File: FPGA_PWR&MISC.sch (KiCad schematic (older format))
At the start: 95 parts, among them Q19 BSS139, U1 XC7A200T-FBG484

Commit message: SW2 placement changed, BOM cleared, FPGA boot, less ERC errors and wornings
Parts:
- removed R160: R0402_1K_1%_0.0625W_100PPM, RESC1005X40N, symbol Resistors_SMD:R0402_1K_1%_0.0625W_100PPM
- added R160: R0402_2K2_1%_0.0625W_100PPM, RESC1005X40N, symbol Resistors_SMD:R0402_2K2_1%_0.0625W_100PPM
- added R282: R0402_4K7_1%_0.0625W_100PPM, RESC1005X40N, symbol Resistors_SMD:R0402_4K7_1%_0.0625W_100PPM
- added R283, R284, R285: R0402_1K_1%_0.0625W_100PPM, RESC1005X40N, symbol Resistors_SMD:R0402_1K_1%_0.0625W_100PPM
- added R286, R287, R288: R0402_0R_JUMPER, RESC1005X40N, symbol Resistors_SMD:R0402_0R_JUMPER
- R162: config (none) -> dnf; ~ 300 -> DNP
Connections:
- wire segments 369 -> 386
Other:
- moved on the sheet: LD3, Q19, R159, R161, R162, R163

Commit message: BOM updated, 25MHz clock level fixed
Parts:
- PB1: symbol AMC_FMC_Carrier-PcbDoc-rescue:PB_TYCO_FSM2JSMA-Switches -> AMC_FMC_Carrier-PcbDoc-rescue:PB_TYCO_FSM2JSMA-Switches-AMC_FMC_Carrier-PcbDoc-rescue
- U1: symbol AMC_FMC_Carrier-PcbDoc-rescue:XC7A200T-FBG484-FPGA_Xilinx_Artix7 -> AMC_FMC_Carrier-PcbDoc-rescue:XC7A200T-FBG484-FPGA_Xilinx_Artix7-AMC_FMC_Carrier-PcbDoc-rescue
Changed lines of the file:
@@
 $EndDescr
 $Comp
-L AMC_FMC_Carrier-PcbDoc-rescue:XC7A200T-FBG484-FPGA_Xilinx_Artix7 U?
+L AMC_FMC_Carrier-PcbDoc-rescue:XC7A200T-FBG484-FPGA_Xilinx_Artix7-AMC_FMC_Carrier-PcbDoc-rescue U?
 U 5 1 5C5BFA2D
 P 11000 2150
@@
 $EndComp
 $Comp
-L AMC_FMC_Carrier-PcbDoc-rescue:XC7A200T-FBG484-FPGA_Xilinx_Artix7 U?
+L AMC_FMC_Carrier-PcbDoc-rescue:XC7A200T-FBG484-FPGA_Xilinx_Artix7-AMC_FMC_Carrier-PcbDoc-rescue U?
 U 6 1 5C5BFA33
 P 8450 5750
@@
 $EndComp
 $Comp
-L AMC_FMC_Carrier-PcbDoc-rescue:XC7A200T-FBG484-FPGA_Xilinx_Artix7 U?
+L AMC_FMC_Carrier-PcbDoc-rescue:XC7A200T-FBG484-FPGA_Xilinx_Artix7-AMC_FMC_Carrier-PcbDoc-rescue U?
 U 7 1 5C5BFA39
 P 3650 4450
@@
 	4700 2750 4700 2650
 $Comp
-L AMC_FMC_Carrier-PcbDoc-rescue:MGTAVCC-powerMG #PWR0440
+L AMC_FMC_Carrier-PcbDoc-rescue:MGTAVCC-powerMG-AMC_FMC_Carrier-PcbDoc-rescue #PWR0440
 U 1 1 5C5F4F86
 P 9450 1700
@@
 $EndComp
 $Comp
-L AMC_FMC_Carrier-PcbDoc-rescue:MGTAVTT-powerMG #PWR0426
+L AMC_FMC_Carrier-PcbDoc-rescue:MGTAVTT-powerMG-AMC_FMC_Carrier-PcbDoc-rescue #PWR0426
 U 1 1 5C5F55FB
 P 3250 9400
@@
 	12500 2150 12550 2150
 $Comp
-L AMC_FMC_Carrier-PcbDoc-rescue:VCCAUX-powerMG #PWR0420
+L AMC_FMC_Carrier-PcbDoc-rescue:VCCAUX-powerMG-AMC_FMC_Carrier-PcbDoc-rescue #PWR0420
 U 1 1 5C5FF42B
 P 2600 1450
@@
 $EndComp
 $Comp
-L AMC_FMC_Carrier-PcbDoc-rescue:VCCBRAM-powerMG #PWR0419
+L AMC_FMC_Carrier-PcbDoc-rescue:VCCBRAM-powerMG-AMC_FMC_Carrier-PcbDoc-rescue #PWR0419
 U 1 1 5C5FFC63
 P 2300 2450
@@
 	12550 1950 12550 1850
 $Comp
-L AMC_FMC_Carrier-PcbDoc-rescue:MGTAVTT-powerMG #PWR0453
+L AMC_FMC_Carrier-PcbDoc-rescue:MGTAVTT-powerMG-AMC_FMC_Carrier-PcbDoc-rescue #PWR0453
 U 1 1 5C618BA3
 P 13450 2450
@@
 $EndComp
 $Comp
-L AMC_FMC_Carrier-PcbDoc-rescue:VCCAUX-powerMG #PWR0421
+L AMC_FMC_Carrier-PcbDoc-rescue:VCCAUX-powerMG-AMC_FMC_Carrier-PcbDoc-rescue #PWR0421
 U 1 1 5C6DE6AD
 P 2600 10350
@@
 $EndComp
 $Comp
-L AMC_FMC_Carrier-PcbDoc-rescue:VCCBRAM-powerMG #PWR0412
+L AMC_FMC_Carrier-PcbDoc-rescue:VCCBRAM-powerMG-AMC_FMC_Carrier-PcbDoc-rescue #PWR0412
 U 1 1 5C6F2B54
 P 950 10300
@@
 $EndComp
 $Comp
-L AMC_FMC_Carrier-PcbDoc-rescue:MGTAVCC-powerMG #PWR0414
+L AMC_FMC_Carrier-PcbDoc-rescue:MGTAVCC-powerMG-AMC_FMC_Carrier-PcbDoc-rescue #PWR0414
 U 1 1 5C71121E
 P 1350 9400
@@
 	3250 9800 3250 9750
 $Comp
-L AMC_FMC_Carrier-PcbDoc-rescue:MGTAVTT-powerMG #PWR0424
+L AMC_FMC_Carrier-PcbDoc-rescue:MGTAVTT-powerMG-AMC_FMC_Carrier-PcbDoc-rescue #PWR0424
 U 1 1 5C961E72
 P 2800 9400
@@
 	2800 9750 2800 9800
 $Comp
-L AMC_FMC_Carrier-PcbDoc-rescue:MGTAVTT-powerMG #PWR0452
+L AMC_FMC_Carrier-PcbDoc-rescue:MGTAVTT-powerMG-AMC_FMC_Carrier-PcbDoc-rescue #PWR0452
 U 1 1 5C999EFD
 P 12550 1700
@@
 	900  9750 900  9800
 $Comp
-L AMC_FMC_Carrier-PcbDoc-rescue:MGTAVCC-powerMG #PWR0410
+L AMC_FMC_Carrier-PcbDoc-rescue:MGTAVCC-powerMG-AMC_FMC_Carrier-PcbDoc-rescue #PWR0410
 U 1 1 5C9F2FA3
 P 900 9400
@@
 PROG_B
 $Comp
-L AMC_FMC_Carrier-PcbDoc-rescue:PB_TYCO_FSM2JSMA-Switches PB1
+L AMC_FMC_Carrier-PcbDoc-rescue:PB_TYCO_FSM2JSMA-Switches-AMC_FMC_Carrier-PcbDoc-rescue PB1
 U 1 1 5C6A56F0
 P 11350 6550

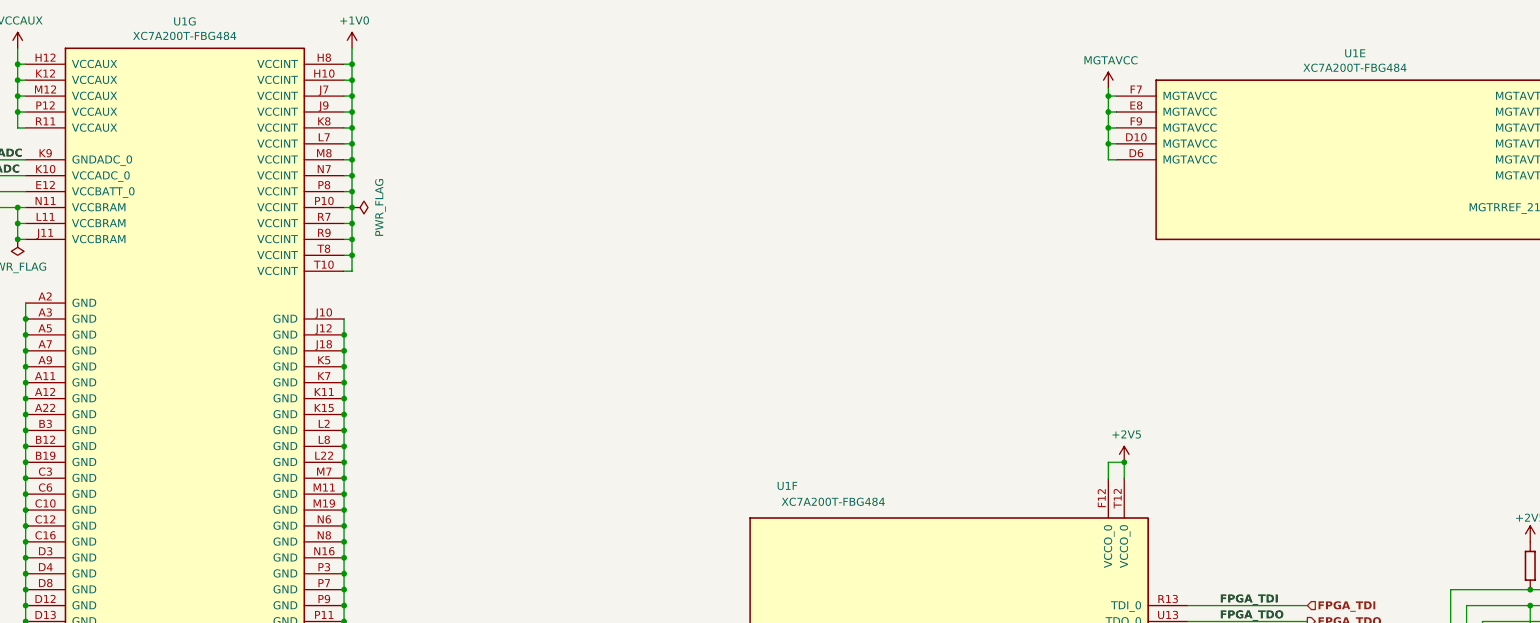
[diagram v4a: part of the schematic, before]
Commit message: BOM configuration file edited, updated Marble picture, some components part number changed
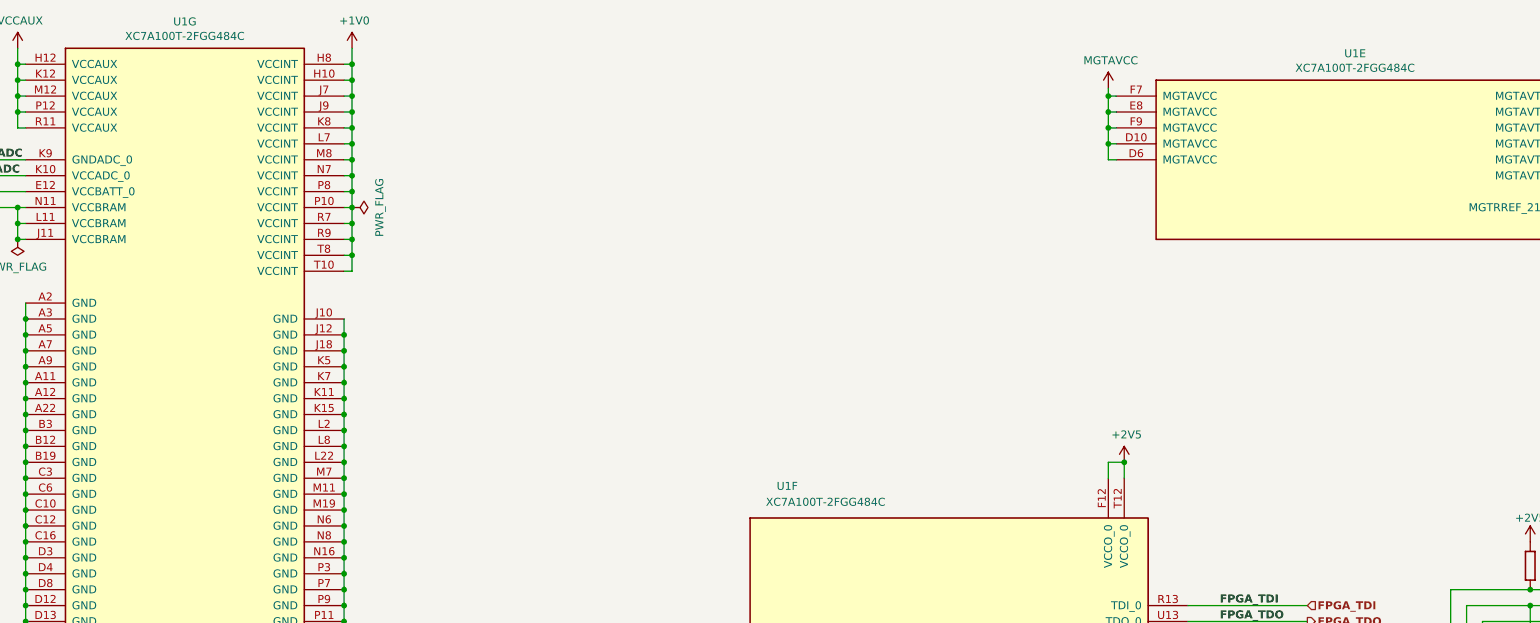
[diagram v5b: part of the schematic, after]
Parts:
- Q19: Manufacturer Part Number BSS139 -> BSS139H6327XTSA1
- U1: value XC7A200T-FBG484 -> XC7A100T-2FGG484C; Manufacturer Part Number (none) -> XC7A100T-2FGG484C
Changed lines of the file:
@@
 $Descr A3 16535 11693
 encoding utf-8
-Sheet 18 25
+Sheet 17 25
 Title "Marble"
 Date "2019-01-16"
@@
 AR Path="/5C907554/5C417BCB/5C5BFA2D" Ref="U1"  Part="5"
 F 0 "U1" H 11000 2817 50  0000 C CNN
-F 1 "XC7A200T-FBG484" H 11000 2726 50  0000 C CNN
+F 1 "XC7A100T-2FGG484C" H 11000 2726 50  0000 C CNN
 F 2 "ICs And Semiconductors SMD_BGA:BGA484C100P22X22_2300X2300X240" H 11000 2150 50  0001 C CNN
 F 3 "" H 11000 2150 50  0000 C CNN
+F 4 "XC7A100T-2FGG484C" H 11000 2150 50  0001 C CNN "Manufacturer Part Number"
 	5    11000 2150
 	1    0    0    -1
@@
 AR Path="/5C907554/5C417BCB/5C5BFA33" Ref="U1"  Part="6"
 F 0 "U1" H 7500 7300 50  0000 R CNN
-F 1 "XC7A200T-FBG484" H 8050 7200 50  0000 R CNN
+F 1 "XC7A100T-2FGG484C" H 8050 7200 50  0000 R CNN
 F 2 "ICs And Semiconductors SMD_BGA:BGA484C100P22X22_2300X2300X240" H 8450 5750 50  0001 C CNN
 F 3 "" H 8450 5750 50  0000 C CNN
+F 4 "XC7A100T-2FGG484C" H 8450 5750 50  0001 C CNN "Manufacturer Part Number"
 	6    8450 5750
 	1    0    0    -1
@@
 AR Path="/5C907554/5C417BCB/5C5BFA39" Ref="U1"  Part="7"
 F 0 "U1" H 3650 7617 50  0000 C CNN
-F 1 "XC7A200T-FBG484" H 3650 7526 50  0000 C CNN
+F 1 "XC7A100T-2FGG484C" H 3650 7526 50  0000 C CNN
 F 2 "ICs And Semiconductors SMD_BGA:BGA484C100P22X22_2300X2300X240" H 3650 4450 50  0001 C CNN
 F 3 "" H 3650 4450 50  0000 C CNN
+F 4 "XC7A100T-2FGG484C" H 3650 4450 50  0001 C CNN "Manufacturer Part Number"
 	7    3650 4450
 	1    0    0    -1
@@
 F 13 "250V 30mA N-Channel  SIPMOS® Small-Signal-Transistor" H 15150 3720 60  0001 L CNN "Part Description"
 F 14 "INFINEON" H 15150 3630 60  0001 L CNN "Manufacturer"
-F 15 "BSS139" H 15150 3540 60  0001 L CNN "Manufacturer Part Number"
+F 15 "BSS139H6327XTSA1" H 15150 3540 60  0001 L CNN "Manufacturer Part Number"
 F 16 "3" H 15150 3450 60  0001 L CNN "Pin Count"
 F 17 "SOT23-3" H 15150 3360 60  0001 L CNN "Case"

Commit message: applied all required amendments to the project
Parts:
- Q19: value BSS139 -> BSS138LT1G; footprint SOT95P240X110-3N -> ICs And Semiconductors SMD:SOT95P240X110-3N; symbol Transistors:BSS139 -> Transistors:BSS138LT1G; Comment =Device -> BSS138LT1G; ComponentHeight 1.1mm -> 1.11mm; ComponentLink1Description ~~ -> (none); ComponentLink2Description ~~ -> (none); CreateDate 09/23/14 00:00:00 -> 03/23/09 00:00:00; Database Table Name (none) -> Transistors; Device BSS139 -> BSS138LT1G; Footprint Library (none) -> ICs And Semiconductors SMD; LatestRevisionDate 09/23/14 00:00:00 -> 03/23/09 00:00:00; Library Name ICs And Semiconductors SMD -> ICs And Semiconductors.DbLib; Manufacturer INFINEON -> ON SEMICONDUCTOR; Manufacturer Part Number BSS139H6327XTSA1 -> BSS138LT1G; Part Description 250V 30mA N-Channel SIPMOS® Small-Signal-Transistor -> 50V 200mA N-Channel Enhancement Mode Field-Effect Transistor; Part Number BSS139 -> BSS138LT1G; SCEM (none) -> (none); Sense Comment ~~ -> (none); Status ~~ -> (none); Status Comment ~~ -> (none)
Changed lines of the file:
@@
 EESchema Schematic File Version 4
 LIBS:AMC_FMC_Carrier-PcbDoc-cache
-EELAYER 29 0
+EELAYER 30 0
 EELAYER END
 $Descr A3 16535 11693
@@
 $EndComp
 $Comp
-L Transistors:BSS139 Q19
+L Transistors:BSS138LT1G Q19
 U 1 1 5D220E28
 P 15150 5200
 F 0 "Q19" H 15469 5296 50  0000 L CNN
-F 1 "BSS139" H 15469 5205 50  0000 L CNN
-F 2 "SOT95P240X110-3N" H 15150 3990 60  0001 L CNN
+F 1 "BSS138LT1G" H 15469 5205 50  0000 L CNN
+F 2 "ICs And Semiconductors SMD:SOT95P240X110-3N" H 15150 3990 60  0001 L CNN
 F 3 "\\\\cern.ch\\dfs\\Applications\\Altium\\Datasheets\\BSS139.pdf" H 15150 4710 60  0001 L CNN
-F 4 "BSS139" H 15150 4620 60  0001 L CNN "Part Number"
+F 4 "BSS138LT1G" H 15150 4620 60  0001 L CNN "Part Number"
 F 5 "N-MOSFET-D 1G 2S 3D" H 15150 4530 60  0001 L CNN "Library Ref"
 F 6 "SchLib\\Transistors.SchLib" H 15150 4440 60  0001 L CNN "Library Path"
-F 7 "=Device" H 15150 4350 60  0001 L CNN "Comment"
+F 7 "BSS138LT1G" H 15150 4350 60  0001 L CNN "Comment"
 F 8 "Standard" H 15150 4260 60  0001 L CNN "Component Kind"
 F 9 "Standard" H 15150 4170 60  0001 L CNN "Component Type"
-F 10 "BSS139" H 15150 4080 60  0001 L CNN "Device"
+F 10 "BSS138LT1G" H 15150 4080 60  0001 L CNN "Device"
 F 11 "SOT23 3-Leads, Pitch 0.95mm - Body 1.4x3mm, IPC Medium Density" H 15150 3900 60  0001 L CNN "PackageDescription"
-F 12 "~~" H 15150 3810 60  0001 L CNN "Status"
-F 13 "250V 30mA N-Channel  SIPMOS® Small-Signal-Transistor" H 15150 3720 60  0001 L CNN "Part Description"
-F 14 "INFINEON" H 15150 3630 60  0001 L CNN "Manufacturer"
-F 15 "BSS139H6327XTSA1" H 15150 3540 60  0001 L CNN "Manufacturer Part Number"
+F 12 " " H 15150 3810 60  0001 L CNN "Status"
+F 13 "50V 200mA N-Channel Enhancement Mode Field-Effect Transistor" H 15150 3720 60  0001 L CNN "Part Description"
+F 14 "ON SEMICONDUCTOR" H 15150 3630 60  0001 L CNN "Manufacturer"
+F 15 "BSS138LT1G" H 15150 3540 60  0001 L CNN "Manufacturer Part Number"
 F 16 "3" H 15150 3450 60  0001 L CNN "Pin Count"
 F 17 "SOT23-3" H 15150 3360 60  0001 L CNN "Case"
@@
 F 21 "Yes" H 15150 3000 60  0001 L CNN "SMD"
 F 22 "No" H 15150 2910 60  0001 L CNN "Sense"
-F 23 "~~" H 15150 2820 60  0001 L CNN "Sense Comment"
+F 23 " " H 15150 2820 60  0001 L CNN "Sense Comment"
 F 24 "No" H 15150 2730 60  0001 L CNN "Bonding"
-F 25 "~~" H 15150 2640 60  0001 L CNN "Status Comment"
-F 26 "1.1mm" H 15150 2550 60  0001 L CNN "ComponentHeight"
+F 25 " " H 15150 2640 60  0001 L CNN "Status Comment"
+F 26 "1.11mm" H 15150 2550 60  0001 L CNN "ComponentHeight"
 F 27 "PcbLib\\ICs And Semiconductors SMD.PcbLib" H 15150 2460 60  0001 L CNN "Footprint Path"
 F 28 "SOT95P240X110-3N" H 15150 2370 60  0001 L CNN "Footprint Ref"
 F 29 "\\\\cern.ch\\dfs\\Applications\\Altium\\Datasheets\\BSS139.pdf" H 15150 2280 60  0001 L CNN "HelpURL"
 F 30 "~~" H 15150 2190 60  0001 L CNN "ComponentLink1URL"
-F 31 "~~" H 15150 2100 60  0001 L CNN "ComponentLink1Description"
+F 31 " " H 15150 2100 60  0001 L CNN "ComponentLink1Description"
 F 32 "~~" H 15150 2010 60  0001 L CNN "ComponentLink2URL"
-F 33 "~~" H 15150 1920 60  0001 L CNN "ComponentLink2Description"
+F 33 " " H 15150 1920 60  0001 L CNN "ComponentLink2Description"
 F 34 "CERN DEM JLC" H 15150 1830 60  0001 L CNN "Author"
-F 35 "09/23/14 00:00:00" H 15150 1740 60  0001 L CNN "CreateDate"
-F 36 "09/23/14 00:00:00" H 15150 1650 60  0001 L CNN "LatestRevisionDate"
-F 37 "ICs And Semiconductors SMD" H 15150 1560 60  0001 L CNN "Library Name"
+F 35 "03/23/09 00:00:00" H 15150 1740 60  0001 L CNN "CreateDate"
+F 36 "03/23/09 00:00:00" H 15150 1650 60  0001 L CNN "LatestRevisionDate"
+F 37 "ICs And Semiconductors.DbLib" H 15150 1560 60  0001 L CNN "Library Name"
 F 38 "This work is licensed under the Creative Commons CC-BY-SA 4.0 License. To the extent that circuit schematics that use Licensed Material can be considered to be ‘Adapted Material’, then the copyright holder waives article 3.b of the license with respect to these schematics." H 15150 1470 60  0001 L CNN "License"
+F 39 "Transistors" H 15150 5200 50  0001 C CNN "Database Table Name"
+F 40 "ICs And Semiconductors SMD" H 15150 5200 50  0001 C CNN "Footprint Library"
+F 41 " " H 15150 5200 50  0001 C CNN "SCEM"
 	1    15150 5200
 	1    0    0    -1

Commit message: Rename library AMC_FMC_Carrier-PcbDoc-rescue as marble_misc
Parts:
- PB1: symbol AMC_FMC_Carrier-PcbDoc-rescue:PB_TYCO_FSM2JSMA-Switches-AMC_FMC_Carrier-PcbDoc-rescue -> marble_misc:PB_TYCO_FSM2JSMA-Switches-AMC_FMC_Carrier-PcbDoc-rescue
- U1: symbol AMC_FMC_Carrier-PcbDoc-rescue:XC7A200T-FBG484-FPGA_Xilinx_Artix7-AMC_FMC_Carrier-PcbDoc-rescue -> marble_misc:XC7A200T-FBG484-FPGA_Xilinx_Artix7-AMC_FMC_Carrier-PcbDoc-rescue
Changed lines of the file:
@@
 $EndDescr
 $Comp
-L AMC_FMC_Carrier-PcbDoc-rescue:XC7A200T-FBG484-FPGA_Xilinx_Artix7-AMC_FMC_Carrier-PcbDoc-rescue U?
+L marble_misc:XC7A200T-FBG484-FPGA_Xilinx_Artix7-AMC_FMC_Carrier-PcbDoc-rescue U?
 U 5 1 5C5BFA2D
 P 11000 2150
@@
 $EndComp
 $Comp
-L AMC_FMC_Carrier-PcbDoc-rescue:XC7A200T-FBG484-FPGA_Xilinx_Artix7-AMC_FMC_Carrier-PcbDoc-rescue U?
+L marble_misc:XC7A200T-FBG484-FPGA_Xilinx_Artix7-AMC_FMC_Carrier-PcbDoc-rescue U?
 U 6 1 5C5BFA33
 P 8450 5750
@@
 $EndComp
 $Comp
-L AMC_FMC_Carrier-PcbDoc-rescue:XC7A200T-FBG484-FPGA_Xilinx_Artix7-AMC_FMC_Carrier-PcbDoc-rescue U?
+L marble_misc:XC7A200T-FBG484-FPGA_Xilinx_Artix7-AMC_FMC_Carrier-PcbDoc-rescue U?
 U 7 1 5C5BFA39
 P 3650 4450
@@
 	4700 2750 4700 2650
 $Comp
-L AMC_FMC_Carrier-PcbDoc-rescue:MGTAVCC-powerMG-AMC_FMC_Carrier-PcbDoc-rescue #PWR0440
+L marble_misc:MGTAVCC-powerMG-AMC_FMC_Carrier-PcbDoc-rescue #PWR0440
 U 1 1 5C5F4F86
 P 9450 1700
@@
 $EndComp
 $Comp
-L AMC_FMC_Carrier-PcbDoc-rescue:MGTAVTT-powerMG-AMC_FMC_Carrier-PcbDoc-rescue #PWR0426
+L marble_misc:MGTAVTT-powerMG-AMC_FMC_Carrier-PcbDoc-rescue #PWR0426
 U 1 1 5C5F55FB
 P 3250 9400
@@
 	12500 2150 12550 2150
 $Comp
-L AMC_FMC_Carrier-PcbDoc-rescue:VCCAUX-powerMG-AMC_FMC_Carrier-PcbDoc-rescue #PWR0420
+L marble_misc:VCCAUX-powerMG-AMC_FMC_Carrier-PcbDoc-rescue #PWR0420
 U 1 1 5C5FF42B
 P 2600 1450
@@
 $EndComp
 $Comp
-L AMC_FMC_Carrier-PcbDoc-rescue:VCCBRAM-powerMG-AMC_FMC_Carrier-PcbDoc-rescue #PWR0419
+L marble_misc:VCCBRAM-powerMG-AMC_FMC_Carrier-PcbDoc-rescue #PWR0419
 U 1 1 5C5FFC63
 P 2300 2450
@@
 	12550 1950 12550 1850
 $Comp
-L AMC_FMC_Carrier-PcbDoc-rescue:MGTAVTT-powerMG-AMC_FMC_Carrier-PcbDoc-rescue #PWR0453
+L marble_misc:MGTAVTT-powerMG-AMC_FMC_Carrier-PcbDoc-rescue #PWR0453
 U 1 1 5C618BA3
 P 13450 2450
@@
 $EndComp
 $Comp
-L AMC_FMC_Carrier-PcbDoc-rescue:VCCAUX-powerMG-AMC_FMC_Carrier-PcbDoc-rescue #PWR0421
+L marble_misc:VCCAUX-powerMG-AMC_FMC_Carrier-PcbDoc-rescue #PWR0421
 U 1 1 5C6DE6AD
 P 2600 10350
@@
 $EndComp
 $Comp
-L AMC_FMC_Carrier-PcbDoc-rescue:VCCBRAM-powerMG-AMC_FMC_Carrier-PcbDoc-rescue #PWR0412
+L marble_misc:VCCBRAM-powerMG-AMC_FMC_Carrier-PcbDoc-rescue #PWR0412
 U 1 1 5C6F2B54
 P 950 10300
@@
 $EndComp
 $Comp
-L AMC_FMC_Carrier-PcbDoc-rescue:MGTAVCC-powerMG-AMC_FMC_Carrier-PcbDoc-rescue #PWR0414
+L marble_misc:MGTAVCC-powerMG-AMC_FMC_Carrier-PcbDoc-rescue #PWR0414
 U 1 1 5C71121E
 P 1350 9400
@@
 	3250 9800 3250 9750
 $Comp
-L AMC_FMC_Carrier-PcbDoc-rescue:MGTAVTT-powerMG-AMC_FMC_Carrier-PcbDoc-rescue #PWR0424
+L marble_misc:MGTAVTT-powerMG-AMC_FMC_Carrier-PcbDoc-rescue #PWR0424
 U 1 1 5C961E72
 P 2800 9400
@@
 	2800 9750 2800 9800
 $Comp
-L AMC_FMC_Carrier-PcbDoc-rescue:MGTAVTT-powerMG-AMC_FMC_Carrier-PcbDoc-rescue #PWR0452
+L marble_misc:MGTAVTT-powerMG-AMC_FMC_Carrier-PcbDoc-rescue #PWR0452
 U 1 1 5C999EFD
 P 12550 1700
@@
 	900  9750 900  9800
 $Comp
-L AMC_FMC_Carrier-PcbDoc-rescue:MGTAVCC-powerMG-AMC_FMC_Carrier-PcbDoc-rescue #PWR0410
+L marble_misc:MGTAVCC-powerMG-AMC_FMC_Carrier-PcbDoc-rescue #PWR0410
 U 1 1 5C9F2FA3
 P 900 9400
@@
 PROG_B
 $Comp
-L AMC_FMC_Carrier-PcbDoc-rescue:PB_TYCO_FSM2JSMA-Switches-AMC_FMC_Carrier-PcbDoc-rescue PB1
+L marble_misc:PB_TYCO_FSM2JSMA-Switches-AMC_FMC_Carrier-PcbDoc-rescue PB1
 U 1 1 5C6A56F0
 P 11350 6550

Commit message: Strip extraneous AMC_FMC_Carrier-PcbDoc-rescue and powerMG from symbol names
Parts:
- PB1: symbol marble_misc:PB_TYCO_FSM2JSMA-Switches-AMC_FMC_Carrier-PcbDoc-rescue -> marble_misc:PB_TYCO_FSM2JSMA-Switches
- U1: symbol marble_misc:XC7A200T-FBG484-FPGA_Xilinx_Artix7-AMC_FMC_Carrier-PcbDoc-rescue -> marble_misc:XC7A200T-FBG484-FPGA_Xilinx_Artix7
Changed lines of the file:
@@
 $EndDescr
 $Comp
-L marble_misc:XC7A200T-FBG484-FPGA_Xilinx_Artix7-AMC_FMC_Carrier-PcbDoc-rescue U?
+L marble_misc:XC7A200T-FBG484-FPGA_Xilinx_Artix7 U?
 U 5 1 5C5BFA2D
 P 11000 2150
@@
 $EndComp
 $Comp
-L marble_misc:XC7A200T-FBG484-FPGA_Xilinx_Artix7-AMC_FMC_Carrier-PcbDoc-rescue U?
+L marble_misc:XC7A200T-FBG484-FPGA_Xilinx_Artix7 U?
 U 6 1 5C5BFA33
 P 8450 5750
@@
 $EndComp
 $Comp
-L marble_misc:XC7A200T-FBG484-FPGA_Xilinx_Artix7-AMC_FMC_Carrier-PcbDoc-rescue U?
+L marble_misc:XC7A200T-FBG484-FPGA_Xilinx_Artix7 U?
 U 7 1 5C5BFA39
 P 3650 4450
@@
 	4700 2750 4700 2650
 $Comp
-L marble_misc:MGTAVCC-powerMG-AMC_FMC_Carrier-PcbDoc-rescue #PWR0440
+L marble_misc:MGTAVCC #PWR0440
 U 1 1 5C5F4F86
 P 9450 1700
@@
 $EndComp
 $Comp
-L marble_misc:MGTAVTT-powerMG-AMC_FMC_Carrier-PcbDoc-rescue #PWR0426
+L marble_misc:MGTAVTT #PWR0426
 U 1 1 5C5F55FB
 P 3250 9400
@@
 	12500 2150 12550 2150
 $Comp
-L marble_misc:VCCAUX-powerMG-AMC_FMC_Carrier-PcbDoc-rescue #PWR0420
+L marble_misc:VCCAUX #PWR0420
 U 1 1 5C5FF42B
 P 2600 1450
@@
 $EndComp
 $Comp
-L marble_misc:VCCBRAM-powerMG-AMC_FMC_Carrier-PcbDoc-rescue #PWR0419
+L marble_misc:VCCBRAM #PWR0419
 U 1 1 5C5FFC63
 P 2300 2450
@@
 	12550 1950 12550 1850
 $Comp
-L marble_misc:MGTAVTT-powerMG-AMC_FMC_Carrier-PcbDoc-rescue #PWR0453
+L marble_misc:MGTAVTT #PWR0453
 U 1 1 5C618BA3
 P 13450 2450
@@
 $EndComp
 $Comp
-L marble_misc:VCCAUX-powerMG-AMC_FMC_Carrier-PcbDoc-rescue #PWR0421
+L marble_misc:VCCAUX #PWR0421
 U 1 1 5C6DE6AD
 P 2600 10350
@@
 $EndComp
 $Comp
-L marble_misc:VCCBRAM-powerMG-AMC_FMC_Carrier-PcbDoc-rescue #PWR0412
+L marble_misc:VCCBRAM #PWR0412
 U 1 1 5C6F2B54
 P 950 10300
@@
 $EndComp
 $Comp
-L marble_misc:MGTAVCC-powerMG-AMC_FMC_Carrier-PcbDoc-rescue #PWR0414
+L marble_misc:MGTAVCC #PWR0414
 U 1 1 5C71121E
 P 1350 9400
@@
 	3250 9800 3250 9750
 $Comp
-L marble_misc:MGTAVTT-powerMG-AMC_FMC_Carrier-PcbDoc-rescue #PWR0424
+L marble_misc:MGTAVTT #PWR0424
 U 1 1 5C961E72
 P 2800 9400
@@
 	2800 9750 2800 9800
 $Comp
-L marble_misc:MGTAVTT-powerMG-AMC_FMC_Carrier-PcbDoc-rescue #PWR0452
+L marble_misc:MGTAVTT #PWR0452
 U 1 1 5C999EFD
 P 12550 1700
@@
 	900  9750 900  9800
 $Comp
-L marble_misc:MGTAVCC-powerMG-AMC_FMC_Carrier-PcbDoc-rescue #PWR0410
+L marble_misc:MGTAVCC #PWR0410
 U 1 1 5C9F2FA3
 P 900 9400
@@
 PROG_B
 $Comp
-L marble_misc:PB_TYCO_FSM2JSMA-Switches-AMC_FMC_Carrier-PcbDoc-rescue PB1
+L marble_misc:PB_TYCO_FSM2JSMA-Switches PB1
 U 1 1 5C6A56F0
 P 11350 6550
